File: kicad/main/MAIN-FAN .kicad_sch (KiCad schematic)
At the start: 9 parts, among them J14 MAIN-FAN, Q1 AO4407A, Q9 IRLML6344TRPBF

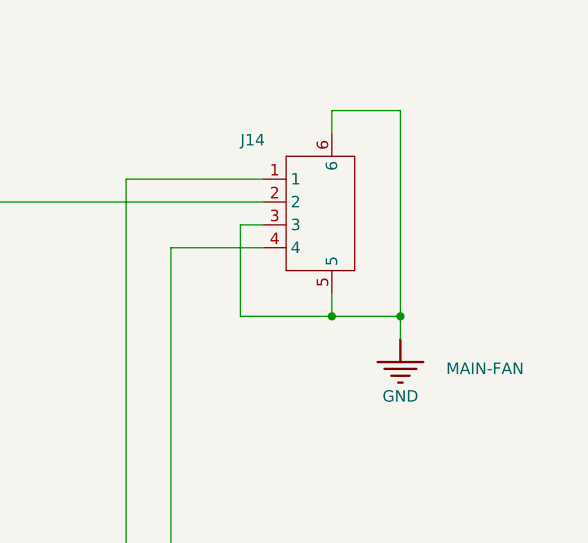
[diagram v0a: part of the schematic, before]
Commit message: Fix edge cut; no-CM STEP
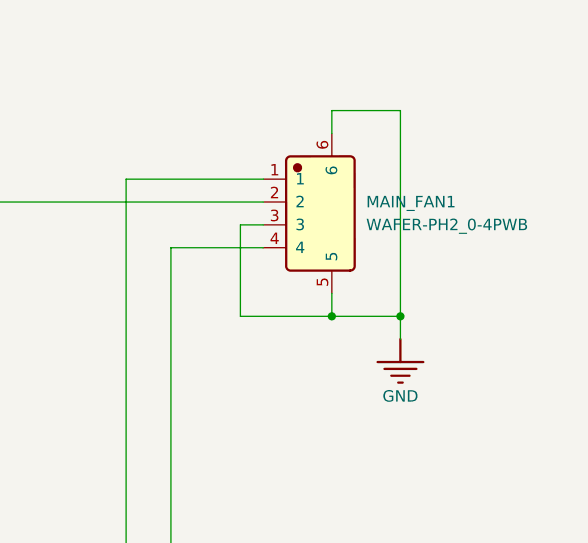
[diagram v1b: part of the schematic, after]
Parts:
- removed J14: MAIN-FAN, oomwoo_altium:CONN-SMD_4P-P2.00_XUNPU_WAFER-PH2.0-4PWB, symbol DesignLibrary:MAIN-FAN_0_HDRx4_DesignLibrary.SchLib
- added MAIN_FAN1: WAFER-PH2_0-4PWB, JLCImport:WAFER-PH2_0-4PWB, symbol JLCImport:WAFER-PH2_0-4PWB
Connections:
- net GND: now also MAIN_FAN1.3, MAIN_FAN1.5, MAIN_FAN1.6
- net MAIN-FAN-S-SENSE: now also MAIN_FAN1.4
- net at R118.1, R119.2: now also MAIN_FAN1.1
- net at D30.2 (K), Q1.5 (D), Q1.6 (D)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: now also MAIN_FAN1.2
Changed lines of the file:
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@@
 		)
 		(instances
-			(project "oomwoo-kicad"
+			(project "Main"
 				(path "/dbcfb655-8d45-4808-9a74-2a0eb03372e8/43bddca0-8e54-471a-b352-8abb91be7702"
 					(reference "#PWR0588")
@@
 		)
 		(instances
-			(project "oomwoo-kicad"
+			(project "Main"
 				(path "/dbcfb655-8d45-4808-9a74-2a0eb03372e8/43bddca0-8e54-471a-b352-8abb91be7702"
 					(reference "R118")
@@
 		)
 		(instances
-			(project "oomwoo-kicad"
+			(project "Main"
 				(path "/dbcfb655-8d45-4808-9a74-2a0eb03372e8/43bddca0-8e54-471a-b352-8abb91be7702"
 					(reference "#PWR0606")
@@
 		)
 		(instances
-			(project "oomwoo-kicad"
+			(project "Main"
 				(path "/dbcfb655-8d45-4808-9a74-2a0eb03372e8/43bddca0-8e54-471a-b352-8abb91be7702"
 					(reference "C101")
+					(unit 1)
+				)
+			)
+		)
+	)
+	(symbol
+		(lib_id "JLCImport:WAFER-PH2_0-4PWB")
+		(at 426.085 127.635 0)
+		(unit 1)
+		(body_style 1)
+		(exclude_from_sim no)
+		(in_bom yes)
+		(on_board yes)
+		(in_pos_files yes)
+		(dnp no)
+		(fields_autoplaced yes)
+		(property "Reference" "MAIN_FAN1"
+			(at 432.435 125.0949 0)
+			(show_name no)
+			(do_not_autoplace no)
+			(effects
+				(font
+					(size 1.27 1.27)
+				)
+				(justify left)
+			)
+		)
+		(property "Value" "WAFER-PH2_0-4PWB"
+			(at 432.435 127.6349 0)
+			(show_name no)
+			(do_not_autoplace no)
+			(effects
+				(font
+					(size 1.27 1.27)
+				)
+				(justify left)
+			)
+		)
+		(property "Footprint" "JLCImport:WAFER-PH2_0-4PWB"
+			(at 426.085 127.635 0)
+			(hide yes)
+			(show_name no)
+			(do_not_autoplace no)
+			(effects
+				(font
+					(size 1.27 1.27)
+				)
+			)
+		)
+		(property "Datasheet" "https://wmsc.lcsc.com/wmsc/upload/file/pdf/v2/lcsc/2205271745_XUNPU-WAFER-PH2-0-4PWB_C3029442.pdf"
+			(at 426.085 127.635 0)
+			(hide yes)
+			(show_name no)
+			(do_not_autoplace no)
+			(effects
+				(font
+					(size 1.27 1.27)
+				)
+			)
+		)
+		(property "Description" "-25℃~+85℃ 1 12mm 1x4P 250V 2A 2mm 4 4P 5.6mm 7.59mm Auxiliary Solder Pin Beige Brass LCP PH Surface Mount, Right Angle Tin SMD,P=2mm,卧贴 Wire To Board Connector ROHS"
+			(at 426.085 127.635 0)
+			(hide yes)
+			(show_name no)
+			(do_not_autoplace no)
+			(effects
+				(font
+					(size 1.27 1.27)
+				)
+			)
+		)
+		(property "LCSC" "C3029442"
+			(at 426.085 127.635 0)
+			(hide yes)
+			(show_name no)
+			(do_not_autoplace no)
+			(effects
+				(font
+					(size 1.27 1.27)
+				)
+			)
+		)
+		(property "Manufacturer" "XUNPU"
+			(at 426.085 127.635 0)
+			(hide yes)
+			(show_name no)
+			(do_not_autoplace no)
+			(effects
+				(font
+					(size 1.27 1.27)
+				)
+			)
+		)
+		(property "Manufacturer Part" "WAFER-PH2.0-4PWB"
+			(at 426.085 127.635 0)
+			(hide yes)
+			(show_name no)
+			(do_not_autoplace no)
+			(effects
+				(font
+					(size 1.27 1.27)
+				)
+			)
+		)
+		(pin "1"
+		)
+		(pin "5"
+		)
+		(pin "4"
+		)
+		(pin "2"
+		)
+		(pin "3"
+		)
+		(pin "6"
+		)
+		(instances
+			(project "Main"
+				(path "/dbcfb655-8d45-4808-9a74-2a0eb03372e8/43bddca0-8e54-471a-b352-8abb91be7702"
+					(reference "MAIN_FAN1")
 					(unit 1)
 				)
@@
 		)
 		(instances
-			(project "oomwoo-kicad"
+			(project "Main"
 				(path "/dbcfb655-8d45-4808-9a74-2a0eb03372e8/43bddca0-8e54-471a-b352-8abb91be7702"
 					(reference "#PWR0608")
@@
 		)
 		(instances
-			(project "oomwoo-kicad"
+			(project "Main"
 				(path "/dbcfb655-8d45-4808-9a74-2a0eb03372e8/43bddca0-8e54-471a-b352-8abb91be7702"
 					(reference "R104")
@@
 		)
 		(instances
-			(project "oomwoo-kicad"
+			(project "Main"
 				(path "/dbcfb655-8d45-4808-9a74-2a0eb03372e8/43bddca0-8e54-471a-b352-8abb91be7702"
 					(reference "Q9")
@@
 		)
 		(instances
-			(project "oomwoo-kicad"
+			(project "Main"
 				(path "/dbcfb655-8d45-4808-9a74-2a0eb03372e8/43bddca0-8e54-471a-b352-8abb91be7702"
 					(reference "#PWR0609")
-					(unit 1)
-				)
-			)
-		)
-	)
-	(symbol
-		(lib_id "DesignLibrary:MAIN-FAN_0_HDRx4_DesignLibrary.SchLib")
-		(at 423.545 120.015 90)
-		(unit 1)
-		(body_style 1)
-		(exclude_from_sim no)
-		(in_bom yes)
-		(on_board yes)
-		(in_pos_files yes)
-		(dnp no)
-		(property "Reference" "J14"
-			(at 418.465 117.475 90)
-			(show_name no)
-			(do_not_autoplace no)
-			(effects
-				(font
-					(size 1.27 1.27)
-				)
-				(justify right bottom)
-			)
-		)
-		(property "Value" "MAIN-FAN"
-			(at 441.325 142.875 90)
-			(show_name no)
-			(do_not_autoplace no)
-			(effects
-				(font
-					(size 1.27 1.27)
-				)
-				(justify right bottom)
-			)
-		)
-		(property "Footprint" "oomwoo_altium:CONN-SMD_4P-P2.00_XUNPU_WAFER-PH2.0-4PWB"
-			(at 423.545 120.015 0)
-			(hide yes)
-			(show_name no)
-			(do_not_autoplace no)
-			(effects
-				(font
-					(size 1.27 1.27)
-				)
-			)
-		)
-		(property "Datasheet" ""
-			(at 423.545 120.015 0)
-			(hide yes)
-			(show_name no)
-			(do_not_autoplace no)
-			(effects
-				(font
-					(size 1.27 1.27)
-				)
-			)
-		)
-		(property "Description" ""
-			(at 423.545 120.015 0)
-			(hide yes)
-			(show_name no)
-			(do_not_autoplace no)
-			(effects
-				(font
-					(size 1.27 1.27)
-				)
-			)
-		)
-		(property "MANUFACTURINGPARTNUMBER" "*"
-			(at 422.275 126.365 90)
-			(hide yes)
-			(show_name no)
-			(do_not_autoplace no)
-			(effects
-				(font
-					(size 1.27 1.27)
-				)
-				(justify right bottom)
-			)
-		)
-		(property "MANUFACTURER" "*"
-			(at 422.275 126.365 90)
-			(hide yes)
-			(show_name no)
-			(do_not_autoplace no)
-			(effects
-				(font
-					(size 1.27 1.27)
-				)
-				(justify right bottom)
-			)
-		)
-		(property "SUPPLIERPARTNUMBER" "*"
-			(at 422.275 126.365 90)
-			(hide yes)
-			(show_name no)
-			(do_not_autoplace no)
-			(effects
-				(font
-					(size 1.27 1.27)
-				)
-				(justify right bottom)
-			)
-		)
-		(property "SUPPLIER" "*"
-			(at 422.275 126.365 90)
-			(hide yes)
-			(show_name no)
-			(do_not_autoplace no)
-			(effects
-				(font
-					(size 1.27 1.27)
-				)
-				(justify right bottom)
-			)
-		)
-		(property "VOLTAGERATE" "*"
-			(at 422.275 126.365 90)
-			(hide yes)
-			(show_name no)
-			(do_not_autoplace no)
-			(effects
-				(font
-					(size 1.27 1.27)
-				)
-				(justify right bottom)
-			)
-		)
-		(pin "5"
-		)
-		(pin "6"
-		)
-		(pin "3"
-		)
-		(pin "2"
-		)
-		(pin "1"
-		)
-		(pin "4"
-		)
-		(instances
-			(project "oomwoo-kicad"
-				(path "/dbcfb655-8d45-4808-9a74-2a0eb03372e8/43bddca0-8e54-471a-b352-8abb91be7702"
-					(reference "J14")
 					(unit 1)
 				)
@@
 		)
 		(instances
-			(project "oomwoo-kicad"
+			(project "Main"
 				(path "/dbcfb655-8d45-4808-9a74-2a0eb03372e8/43bddca0-8e54-471a-b352-8abb91be7702"
 					(reference "R103")
@@
 		)
 		(instances
-			(project "oomwoo-kicad"
+			(project "Main"
 				(path "/dbcfb655-8d45-4808-9a74-2a0eb03372e8/43bddca0-8e54-471a-b352-8abb91be7702"
 					(reference "#PWR0627")
@@
 		)
 		(instances
-			(project "oomwoo-kicad"
+			(project "Main"
 				(path "/dbcfb655-8d45-4808-9a74-2a0eb03372e8/43bddca0-8e54-471a-b352-8abb91be7702"
 					(reference "D30")
@@
 		)
 		(instances
-			(project "oomwoo-kicad"
+			(project "Main"
 				(path "/dbcfb655-8d45-4808-9a74-2a0eb03372e8/43bddca0-8e54-471a-b352-8abb91be7702"
 					(reference "R119")
@@
 		)
 		(instances
-			(project "oomwoo-kicad"
+			(project "Main"
 				(path "/dbcfb655-8d45-4808-9a74-2a0eb03372e8/43bddca0-8e54-471a-b352-8abb91be7702"
 					(reference "Q1")

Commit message: Schematic fixes, 1st round of review
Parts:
- removed D30: SS34, oomwoo_altium:SMA, symbol DesignLibrary:MAIN-BRUSH MOTOR_1_DIODE-2_DesignLibrary.SchLib
- removed Q1: AO4407A, JLCImport:AO4407A, symbol JLCImport:AO4407A
- removed Q9: IRLML6344TRPBF, JLCImport:IRLML6344TRPBF, symbol JLCImport:IRLML6344TRPBF
- removed R103: 22K, Resistor_SMD:R_0603_1608Metric, symbol DesignLibrary:MAIN-FAN_0_Resistor-1_DesignLibrary.SchLib
- removed R104: 1K, Resistor_SMD:R_0603_1608Metric, symbol DesignLibrary:MAIN-FAN_0_Resistor-1_DesignLibrary.SchLib
- removed R118: 1K, Resistor_SMD:R_0603_1608Metric, symbol DesignLibrary:MAIN-FAN_2_Resistor-1_DesignLibrary.SchLib
- removed R119: 10K, Resistor_SMD:R_0603_1608Metric, symbol DesignLibrary:MAIN-FAN_1_Resistor-1_DesignLibrary.SchLib
- added C137: 10uF/25V, Capacitor_SMD:C_0603_1608Metric, symbol JLCImport:CL21A106KBYQNNE
- added C7: 150pF/50V, Capacitor_SMD:C_0603_1608Metric, symbol Device:C_Small
- added Q1: 2302V, JLCImport:2302V, symbol JLCImport:2302V
- added R1, R36, R42: 10k, Resistor_SMD:R_0603_1608Metric, symbol Device:R_US
- C101: value 0.1uF -> 150pF/50V; MANUFACTURER * -> (none); Manufacturer (none) -> *; now not fitted
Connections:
- net GND: now also C137.2, C7.2
- net MAIN-FAN-S-CTRL: now also Q1.2 (S), R42.2
- net MAIN-FAN-S-SENSE: now also MAIN_FAN1.1, R1.2; no longer MAIN_FAN1.4
- net VM-VBAT: now also MAIN_FAN1.4, C137.1
- net at MAIN_FAN1.2: now also C7.1, Q1.3 (D), R36.2
- new net VCC-3V3-P: Q1.1 (G), R1.1, R42.1
- new net VCC-5V-REG: R36.1
